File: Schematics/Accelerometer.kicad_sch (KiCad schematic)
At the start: 0 parts

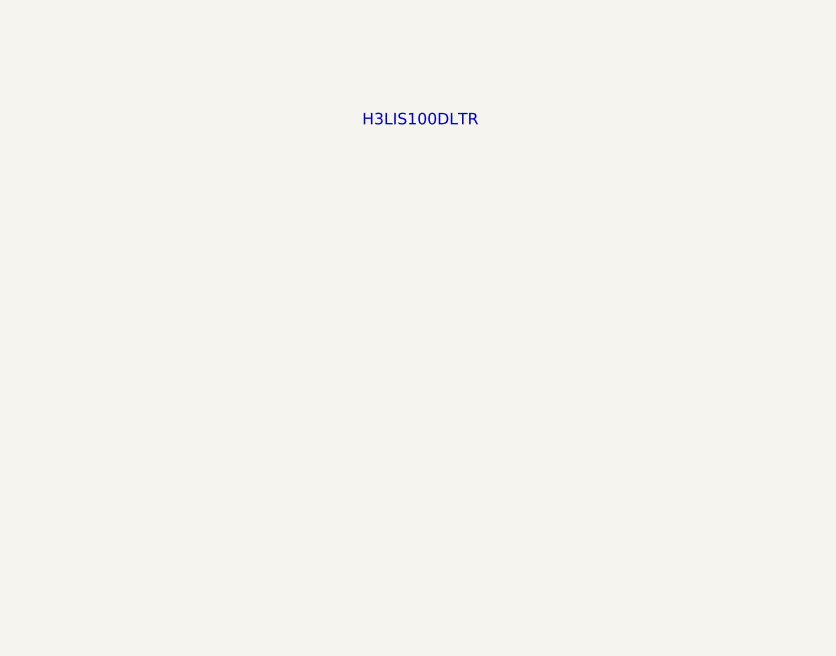
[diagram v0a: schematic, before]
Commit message: finished sensor schematics, added datasheets organized files
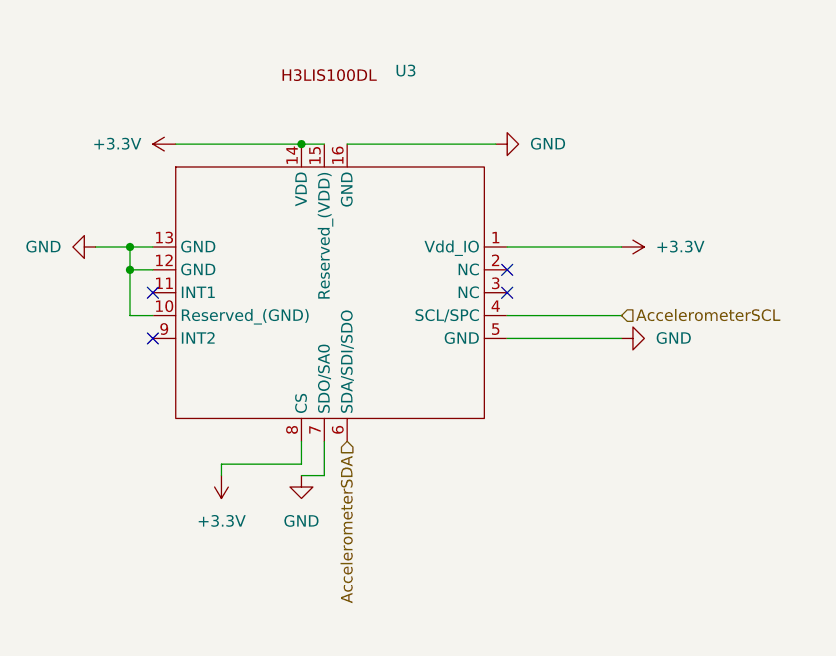
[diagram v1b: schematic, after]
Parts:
- added U3: ~, symbol Footprints:H3LIS100DL
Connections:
- new net +3.3V: U3.1 (Vdd_IO), U3.14 (VDD), U3.15 (Reserved_(VDD)), U3.8 (CS)
- new net AccelerometerSCL: U3.4 (SCL/SPC)
- new net AccelerometerSDA: U3.6 (SDA/SDI/SDO)
- new net GND: U3.10 (Reserved_(GND)), U3.12 (GND), U3.13 (GND), U3.16 (GND), U3.5 (GND), U3.7 (SDO/SA0)
- no-connect marks 0 -> 4
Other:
- note removed: "H3LIS100DLTR"

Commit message: added LCSC numbers and footprint values, need to connect schemeatic pins, then can start layout
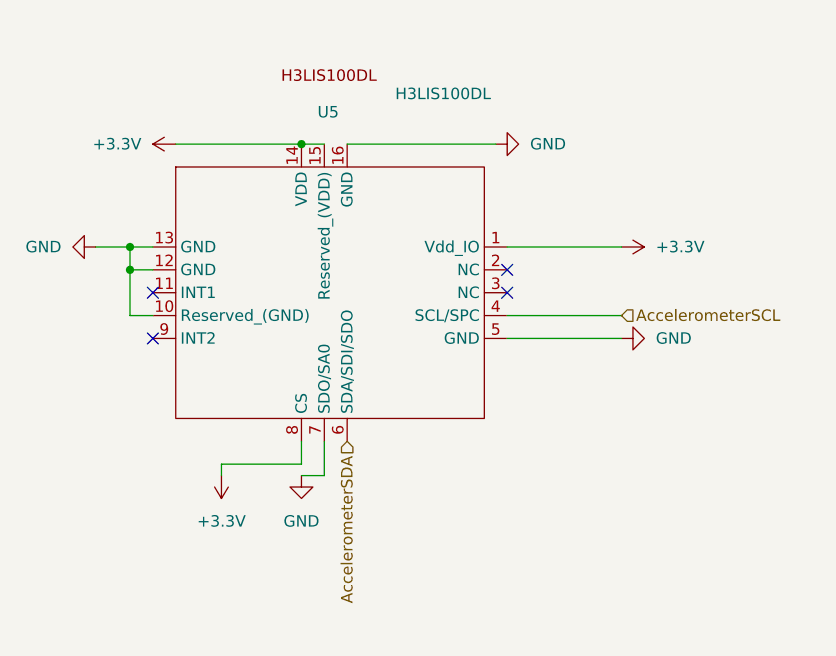
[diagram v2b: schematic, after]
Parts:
- U5: renamed from U3; value ~ -> H3LIS100DL; footprint (none) -> myFootprints:PQFN50P300X300X100-16N; LCSC Part (none) -> C2655068
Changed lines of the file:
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@@
 		(on_board yes)
 		(dnp no)
-		(property "Reference" "U3"
-			(at 156.464 83.312 0)
+		(property "Reference" "U5"
+			(at 147.828 87.884 0)
 			(effects
 				(font
@@
 			)
 		)
-		(property "Value" "~"
+		(property "Value" "H3LIS100DL"
 			(at 156.464 85.852 0)
 			(effects
@@
 			)
 		)
-		(property "Footprint" ""
+		(property "Footprint" "myFootprints:PQFN50P300X300X100-16N"
 			(at 137.16 102.87 0)
 			(effects
@@
 			)
 		)
+		(property "LCSC Part" "C2655068"
+			(at 137.16 102.87 0)
+			(effects
+				(font
+					(size 1.27 1.27)
+				)
+				(hide yes)
+			)
+		)
+		(property "Sim.Device" ""
+			(at 137.16 102.87 0)
+			(effects
+				(font
+					(size 1.27 1.27)
+				)
+				(hide yes)
+			)
+		)
+		(property "Sim.Type" ""
+			(at 137.16 102.87 0)
+			(effects
+				(font
+					(size 1.27 1.27)
+				)
+				(hide yes)
+			)
+		)
 		(pin "2"
 		)
@@
 			(project ""
 				(path "/6cb3dda3-5fe8-4715-b831-354360aa3199/845ef161-5bd7-4496-b5c2-e65e4f30444a"
-					(reference "U3")
+					(reference "U5")
 					(unit 1)
 				)
@@
 		(dnp no)
 		(fields_autoplaced yes)
-		(property "Reference" "#PWR023"
+		(property "Reference" "#PWR079"
 			(at 177.8 102.87 0)
 			(effects
@@
 			(project ""
 				(path "/6cb3dda3-5fe8-4715-b831-354360aa3199/845ef161-5bd7-4496-b5c2-e65e4f30444a"
-					(reference "#PWR023")
+					(reference "#PWR079")
 					(unit 1)
 				)
@@
 		(dnp no)
 		(fields_autoplaced yes)
-		(property "Reference" "#PWR026"
+		(property "Reference" "#PWR074"
 			(at 116.84 102.87 0)
 			(effects
@@
 			(project "flightcomputer2"
 				(path "/6cb3dda3-5fe8-4715-b831-354360aa3199/845ef161-5bd7-4496-b5c2-e65e4f30444a"
-					(reference "#PWR026")
+					(reference "#PWR074")
 					(unit 1)
 				)
@@
 		(dnp no)
 		(fields_autoplaced yes)
-		(property "Reference" "#PWR025"
+		(property "Reference" "#PWR076"
 			(at 137.16 124.46 0)
 			(effects
@@
 			(project "flightcomputer2"
 				(path "/6cb3dda3-5fe8-4715-b831-354360aa3199/845ef161-5bd7-4496-b5c2-e65e4f30444a"
-					(reference "#PWR025")
+					(reference "#PWR076")
 					(unit 1)
 				)
@@
 		(dnp no)
 		(fields_autoplaced yes)
-		(property "Reference" "#PWR074"
+		(property "Reference" "#PWR077"
 			(at 146.05 134.62 0)
 			(effects
@@
 			(project "flightcomputer2"
 				(path "/6cb3dda3-5fe8-4715-b831-354360aa3199/845ef161-5bd7-4496-b5c2-e65e4f30444a"
-					(reference "#PWR074")
+					(reference "#PWR077")
 					(unit 1)
 				)
@@
 		(dnp no)
 		(fields_autoplaced yes)
-		(property "Reference" "#PWR027"
+		(property "Reference" "#PWR078"
 			(at 173.99 91.44 0)
 			(effects
@@
 			(project "flightcomputer2"
 				(path "/6cb3dda3-5fe8-4715-b831-354360aa3199/845ef161-5bd7-4496-b5c2-e65e4f30444a"
-					(reference "#PWR027")
+					(reference "#PWR078")
 					(unit 1)
 				)
@@
 		(dnp no)
 		(fields_autoplaced yes)
-		(property "Reference" "#PWR028"
+		(property "Reference" "#PWR075"
 			(at 135.89 91.44 0)
 			(effects
@@
 			(project "flightcomputer2"
 				(path "/6cb3dda3-5fe8-4715-b831-354360aa3199/845ef161-5bd7-4496-b5c2-e65e4f30444a"
-					(reference "#PWR028")
+					(reference "#PWR075")
 					(unit 1)
 				)
@@
 		(dnp no)
 		(fields_autoplaced yes)
-		(property "Reference" "#PWR024"
+		(property "Reference" "#PWR080"
 			(at 187.96 113.03 0)
 			(effects
@@
 			(project ""
 				(path "/6cb3dda3-5fe8-4715-b831-354360aa3199/845ef161-5bd7-4496-b5c2-e65e4f30444a"
-					(reference "#PWR024")
-					(unit 1)
-				)
+					(reference "#PWR080")
+					(unit 1)
+				)

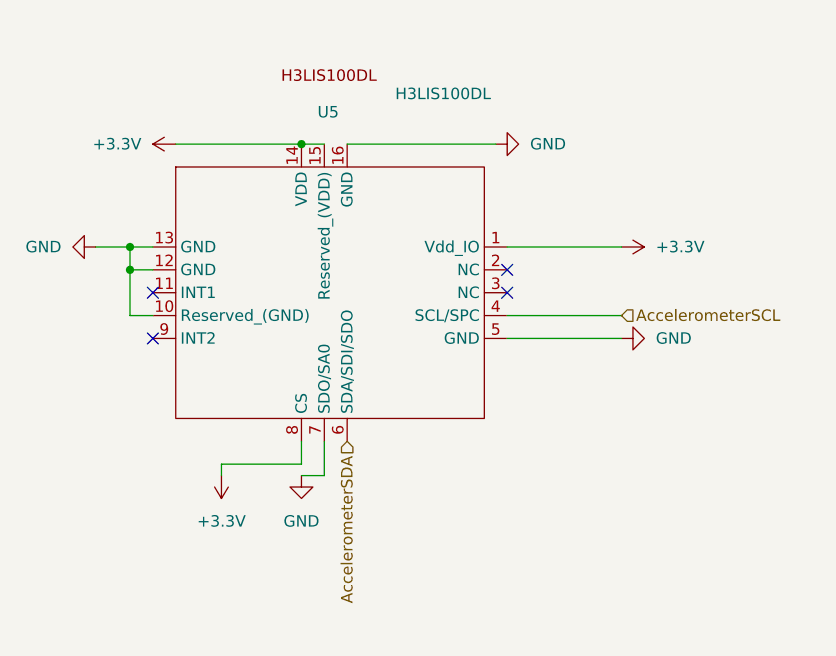
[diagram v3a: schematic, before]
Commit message: fixed symbols and added diodes to power input before ldo
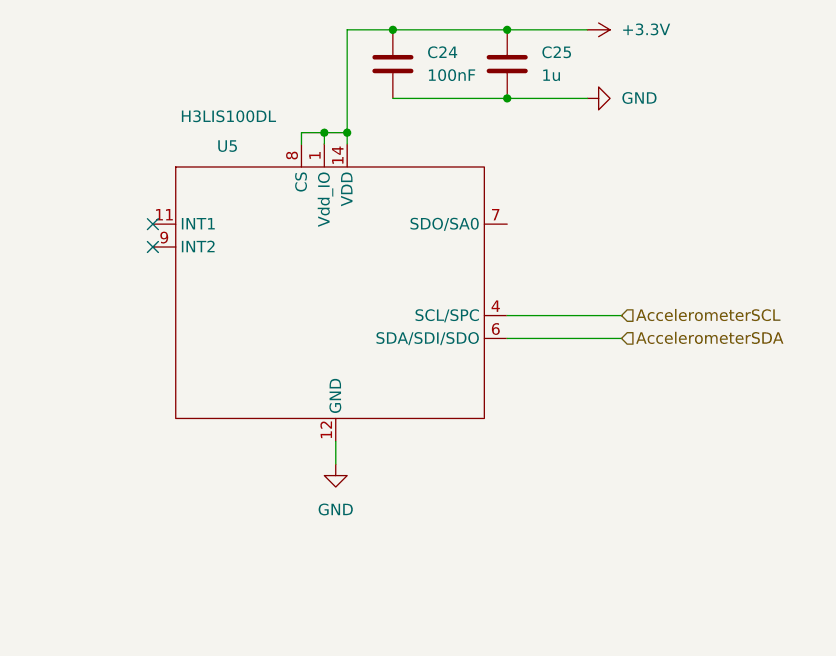
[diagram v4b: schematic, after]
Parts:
- added C24: 100nF, symbol Device:C
- added C25: 1u, symbol Device:C
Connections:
- net +3.3V: now also C24.2, C25.2; no longer U5.15 (Reserved_(VDD))
- net GND: now also C24.1, C25.1; no longer U5.10 (Reserved_(GND)), U5.13 (GND), U5.16 (GND), U5.5 (GND), U5.7 (SDO/SA0)
- no-connect marks 4 -> 2

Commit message: added lora correct and organizing sheet pins
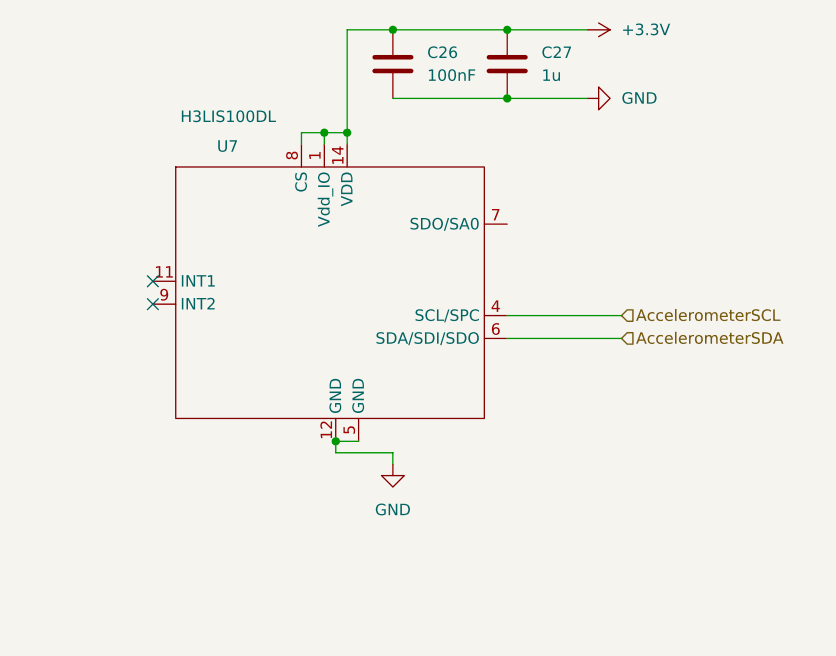
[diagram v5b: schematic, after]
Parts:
- renumbered C24 to C26, C25 to C27, U5 to U7
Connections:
- net GND: now also U7.5 (GND)
- new net VDD: U7.15 (VDD)
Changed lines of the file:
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@@
 		(color 0 0 0 0)
 	)
+	(junction
+		(at 149.86 124.46)
+		(diameter 0)
+		(color 0 0 0 0)
+	)
 	(no_connect
-		(at 129.54 102.87)
+		(at 129.54 109.22)
 	)
 	(no_connect
-		(at 129.54 100.33)
+		(at 129.54 106.68)
 	)
 	(wire
@@
 	(wire
 		(pts
+			(xy 156.21 125.73) (xy 149.86 125.73)
+		)
+		(stroke
+			(width 0)
+			(type default)
+		)
+	)
+	(wire
+		(pts
 			(xy 156.21 78.74) (xy 168.91 78.74)
 		)
@@
 	(wire
 		(pts
+			(xy 149.86 125.73) (xy 149.86 124.46)
+		)
+		(stroke
+			(width 0)
+			(type default)
+		)
+	)
+	(wire
+		(pts
 			(xy 168.91 78.74) (xy 177.8 78.74)
 		)
@@
 	(wire
 		(pts
-			(xy 149.86 124.46) (xy 149.86 127)
+			(xy 156.21 125.73) (xy 156.21 127)
 		)
 		(stroke
@@
 		(pts
 			(xy 148.59 90.17) (xy 151.13 90.17)
+		)
+		(stroke
+			(width 0)
+			(type default)
+		)
+	)
+	(wire
+		(pts
+			(xy 152.4 124.46) (xy 149.86 124.46)
 		)
 		(stroke
@@
 		(dnp no)
 		(fields_autoplaced yes)
-		(property "Reference" "C24"
+		(property "Reference" "C26"
 			(at 160.02 81.2799 0)
 			(effects
@@
 			(project ""
 				(path "/6cb3dda3-5fe8-4715-b831-354360aa3199/845ef161-5bd7-4496-b5c2-e65e4f30444a"
-					(reference "C24")
+					(reference "C26")
 					(unit 1)
 				)
@@
 		(on_board yes)
 		(dnp no)
-		(property "Reference" "U5"
+		(property "Reference" "U7"
 			(at 136.652 91.694 0)
 			(effects
@@
 		)
 		(pin "8"
+		)
+		(pin "3"
+		)
+		(pin "10"
+		)
+		(pin "2"
+		)
+		(pin "15"
+		)
+		(pin "5"
 		)
 		(instances
 			(project ""
 				(path "/6cb3dda3-5fe8-4715-b831-354360aa3199/845ef161-5bd7-4496-b5c2-e65e4f30444a"
-					(reference "U5")
+					(reference "U7")
 					(unit 1)
 				)
@@
 		(dnp no)
 		(fields_autoplaced yes)
-		(property "Reference" "#PWR074"
+		(property "Reference" "#PWR080"
 			(at 184.15 86.36 0)
 			(effects
@@
 			(project ""
 				(path "/6cb3dda3-5fe8-4715-b831-354360aa3199/845ef161-5bd7-4496-b5c2-e65e4f30444a"
-					(reference "#PWR074")
+					(reference "#PWR080")
 					(unit 1)
 				)
@@
 	(symbol
 		(lib_id "power:GND")
-		(at 149.86 127 0)
+		(at 156.21 127 0)
 		(unit 1)
 		(exclude_from_sim no)
@@
 		(dnp no)
 		(fields_autoplaced yes)
-		(property "Reference" "#PWR077"
-			(at 149.86 133.35 0)
+		(property "Reference" "#PWR078"
+			(at 156.21 133.35 0)
 			(effects
 				(font
@@
 		)
 		(property "Value" "GND"
-			(at 149.86 132.08 0)
+			(at 156.21 132.08 0)
 			(effects
 				(font
@@
 		)
 		(property "Footprint" ""
-			(at 149.86 127 0)
+			(at 156.21 127 0)
 			(effects
 				(font
@@
 		)
 		(property "Datasheet" ""
-			(at 149.86 127 0)
+			(at 156.21 127 0)
 			(effects
 				(font
@@
 		)
 		(property "Description" "Power symbol creates a global label with name \"GND\" , ground"
-			(at 149.86 127 0)
+			(at 156.21 127 0)
 			(effects
 				(font
@@
 			(project "flightcomputer2"
 				(path "/6cb3dda3-5fe8-4715-b831-354360aa3199/845ef161-5bd7-4496-b5c2-e65e4f30444a"
-					(reference "#PWR077")
+					(reference "#PWR078")
 					(unit 1)
 				)
@@
 		(dnp no)
 		(fields_autoplaced yes)
-		(property "Reference" "C25"
+		(property "Reference" "C27"
 			(at 172.72 81.2799 0)
 			(effects
@@
 			(project "flightcomputer2"
 				(path "/6cb3dda3-5fe8-4715-b831-354360aa3199/845ef161-5bd7-4496-b5c2-e65e4f30444a"
-					(reference "C25")
+					(reference "C27")
 					(unit 1)
 				)
@@
 		(dnp no)
 		(fields_autoplaced yes)
-		(property "Reference" "#PWR075"
+		(property "Reference" "#PWR079"
 			(at 173.99 78.74 0)
 			(effects
@@
 			(project "flightcomputer2"
 				(path "/6cb3dda3-5fe8-4715-b831-354360aa3199/845ef161-5bd7-4496-b5c2-e65e4f30444a"
-					(reference "#PWR075")
+					(reference "#PWR079")
 					(unit 1)
 				)

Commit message: finished pin assignments and ran ERC all good ready for layout
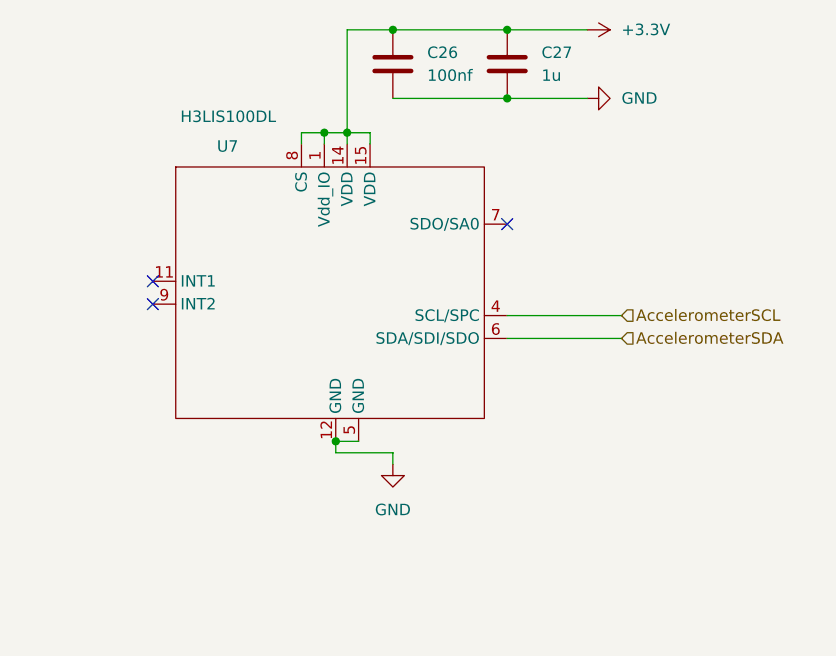
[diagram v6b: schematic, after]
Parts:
- C26: value 100nF -> 100nf; footprint (none) -> Capacitor_SMD:C_0805_2012Metric_Pad1.18x1.45mm_HandSolder; LCSC Part (none) -> C49678
- C27: footprint (none) -> Capacitor_SMD:C_0805_2012Metric_Pad1.18x1.45mm_HandSolder; LCSC Part (none) -> C28323
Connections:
- net VDD is gone; now on net +3.3V: U7.15 (VDD)
- no-connect marks 2 -> 3
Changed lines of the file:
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@@
+	)
+	(no_connect
+		(at 168.91 100.33)
 	)
 	(no_connect
@@
 	(wire
 		(pts
+			(xy 153.67 90.17) (xy 151.13 90.17)
+		)
+		(stroke
+			(width 0)
+			(type default)
+		)
+	)
+	(wire
+		(pts
 			(xy 156.21 78.74) (xy 168.91 78.74)
 		)
@@
 		(pts
 			(xy 151.13 90.17) (xy 151.13 91.44)
+		)
+		(stroke
+			(width 0)
+			(type default)
+		)
+	)
+	(wire
+		(pts
+			(xy 153.67 91.44) (xy 153.67 90.17)
 		)
 		(stroke
@@
 			)
 		)
-		(property "Value" "100nF"
+		(property "Value" "100nf"
 			(at 160.02 83.8199 0)
 			(effects
@@
 			)
 		)
-		(property "Footprint" ""
+		(property "Footprint" "Capacitor_SMD:C_0805_2012Metric_Pad1.18x1.45mm_HandSolder"
 			(at 155.2448 78.74 0)
 			(effects
@@
 		)
 		(property "Description" "Unpolarized capacitor"
+			(at 156.21 82.55 0)
+			(effects
+				(font
+					(size 1.27 1.27)
+				)
+				(hide yes)
+			)
+		)
+		(property "Description_1" ""
+			(at 156.21 82.55 0)
+			(effects
+				(font
+					(size 1.27 1.27)
+				)
+				(hide yes)
+			)
+		)
+		(property "MF" ""
+			(at 156.21 82.55 0)
+			(effects
+				(font
+					(size 1.27 1.27)
+				)
+				(hide yes)
+			)
+		)
+		(property "MP" ""
+			(at 156.21 82.55 0)
+			(effects
+				(font
+					(size 1.27 1.27)
+				)
+				(hide yes)
+			)
+		)
+		(property "Package" ""
+			(at 156.21 82.55 0)
+			(effects
+				(font
+					(size 1.27 1.27)
+				)
+				(hide yes)
+			)
+		)
+		(property "Price" ""
+			(at 156.21 82.55 0)
+			(effects
+				(font
+					(size 1.27 1.27)
+				)
+				(hide yes)
+			)
+		)
+		(property "Purchase-URL" ""
+			(at 156.21 82.55 0)
+			(effects
+				(font
+					(size 1.27 1.27)
+				)
+				(hide yes)
+			)
+		)
+		(property "LCSC Part" "C49678"
 			(at 156.21 82.55 0)
 			(effects
@@
 		(property "LCSC Part" "C2655068"
 			(at 105.41 100.584 0)
+			(effects
+				(font
+					(size 1.27 1.27)
+				)
+				(hide yes)
+			)
+		)
+		(property "Description_1" ""
+			(at 137.16 102.87 0)
+			(effects
+				(font
+					(size 1.27 1.27)
+				)
+				(hide yes)
+			)
+		)
+		(property "MF" ""
+			(at 137.16 102.87 0)
+			(effects
+				(font
+					(size 1.27 1.27)
+				)
+				(hide yes)
+			)
+		)
+		(property "MP" ""
+			(at 137.16 102.87 0)
+			(effects
+				(font
+					(size 1.27 1.27)
+				)
+				(hide yes)
+			)
+		)
+		(property "Package" ""
+			(at 137.16 102.87 0)
+			(effects
+				(font
+					(size 1.27 1.27)
+				)
+				(hide yes)
+			)
+		)
+		(property "Price" ""
+			(at 137.16 102.87 0)
+			(effects
+				(font
+					(size 1.27 1.27)
+				)
+				(hide yes)
+			)
+		)
+		(property "Purchase-URL" ""
+			(at 137.16 102.87 0)
 			(effects
 				(font
@@
 			)
 		)
-		(property "Footprint" ""
+		(property "Footprint" "Capacitor_SMD:C_0805_2012Metric_Pad1.18x1.45mm_HandSolder"
 			(at 167.9448 78.74 0)
 			(effects
@@
 			(at 168.91 82.55 0)
 			(effects
+				(font
+					(size 1.27 1.27)
+				)
+				(hide yes)
+			)
+		)
+		(property "Description_1" ""
+			(at 168.91 82.55 0)
+			(effects
+				(font
+					(size 1.27 1.27)
+				)
+				(hide yes)
+			)
+		)
+		(property "MF" ""
+			(at 168.91 82.55 0)
+			(effects
+				(font
+					(size 1.27 1.27)
+				)
+				(hide yes)
+			)
+		)
+		(property "MP" ""
+			(at 168.91 82.55 0)
+			(effects
+				(font
+					(size 1.27 1.27)
+				)
+				(hide yes)
+			)
+		)
+		(property "Package" ""
+			(at 168.91 82.55 0)
+			(effects
+				(font
+					(size 1.27 1.27)
+				)
+				(hide yes)
+			)
+		)
+		(property "Price" ""
+			(at 168.91 82.55 0)
+			(effects
+				(font
+					(size 1.27 1.27)
+				)
+				(hide yes)
+			)
+		)
+		(property "Purchase-URL" ""
+			(at 168.91 82.55 0)
+			(effects
+				(font
+					(size 1.27 1.27)
+				)
+				(hide yes)
+			)
+		)
+		(property "LCSC Part" "C28323"
+			(at 168.91 82.55 0)
+			(effects
